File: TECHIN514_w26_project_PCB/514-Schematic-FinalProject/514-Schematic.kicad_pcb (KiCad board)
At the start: 2 copper layers, 138 x 62 mm, 15 parts, among them J1 Conn_01x02, U1 28BYJ-48, U2 MPU-6050, U3 ULN2003, U4 ESP32C3, U5 ESP32C3, U6 SSD1306

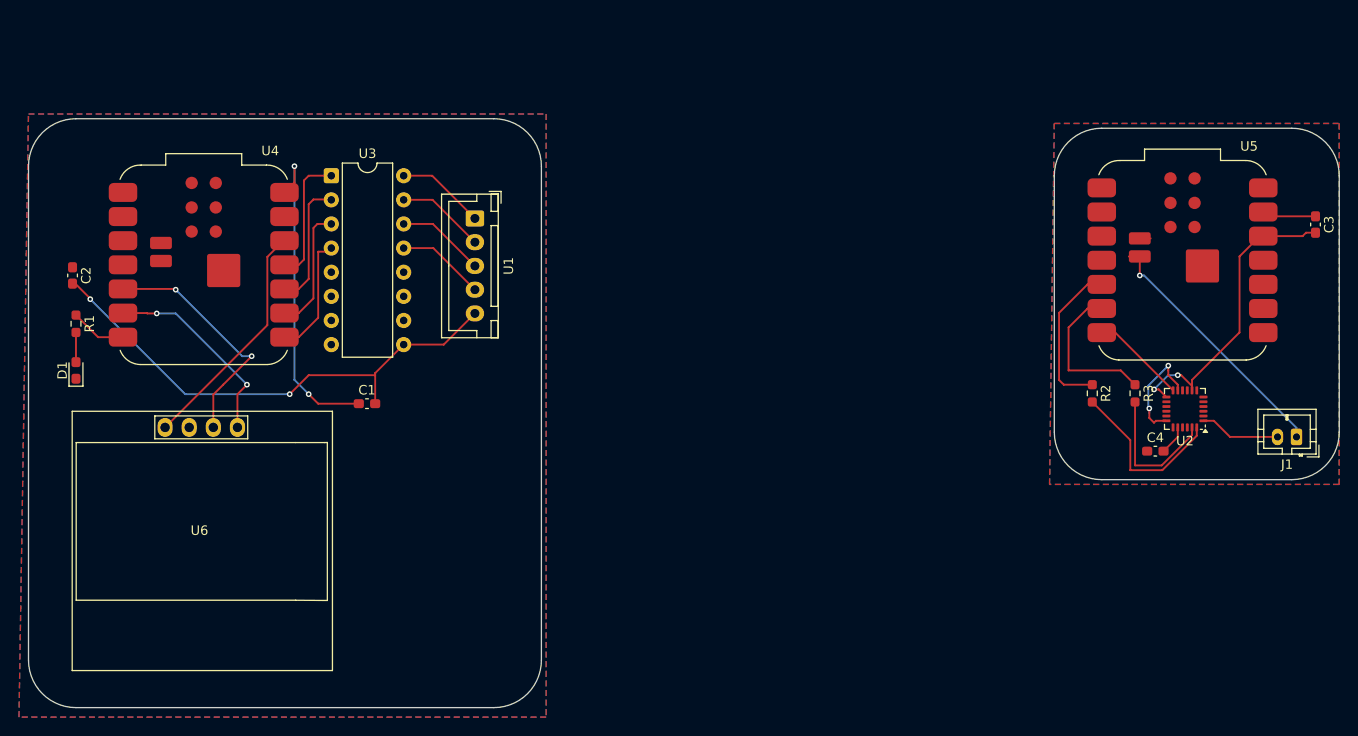
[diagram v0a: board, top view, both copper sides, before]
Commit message: Add PCB and Code for Devices
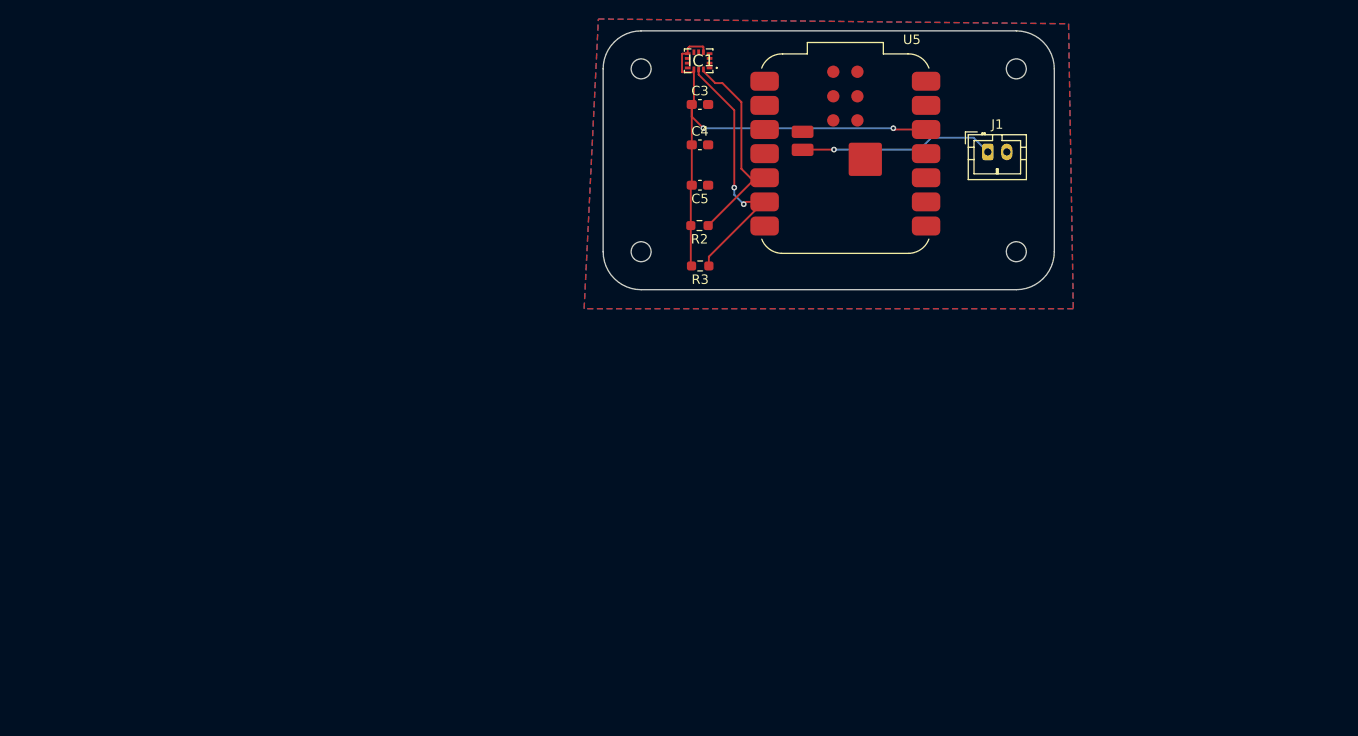
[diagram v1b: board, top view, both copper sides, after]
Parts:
- removed C1: 470uF, Capacitor_SMD:C_0603_1608Metric_Pad1.08x0.95mm_HandSolder
- removed C2: 0.1 uF, Capacitor_SMD:C_0603_1608Metric_Pad1.08x0.95mm_HandSolder
- removed D1: LED, LED_SMD:LED_0603_1608Metric_Pad1.05x0.95mm_HandSolder
- removed R1: 330V, Resistor_SMD:R_0603_1608Metric_Pad0.98x0.95mm_HandSolder
- removed U1: 28BYJ-48, Connector_JST:JST_XH_B5B-XH-A_1x05_P2.50mm_Vertical
- removed U2: MPU-6050, Sensor_Motion:InvenSense_QFN-24_4x4mm_P0.5mm
- removed U3: ULN2003, Package_DIP:DIP-16_W7.62mm
- removed U4: ESP32C3, RF_Module:MCU_Seeed_ESP32C3
- removed U6: SSD1306, Footprints:128x64OLED
- added C5: 10 nF, Capacitor_SMD:C_0603_1608Metric_Pad1.08x0.95mm_HandSolder, F.Cu at (177.7, 66.0)
- added IC1: ICM-42670-P, IMU:ICM42670P, F.Cu at (177.6, 52.9)
- added REF**: MountingHole_2.1mm, MountingHole:MountingHole_2.1mm, F.Cu at (171.5, 53.8)
- added REF**: MountingHole_2.1mm, MountingHole:MountingHole_2.1mm, F.Cu at (211.0, 73.0)
- added REF**: MountingHole_2.1mm, MountingHole:MountingHole_2.1mm, F.Cu at (171.5, 73.0)
- added REF**: MountingHole_2.1mm, MountingHole:MountingHole_2.1mm, F.Cu at (211.0, 53.8)
- C4: value 2.2 nF -> 2.2 uF
- R2, R3: value 4.7k -> 10 kΩ
- moved C3 66.0 mm to (177.7, 57.5), turned to 0 degrees
- moved C4 57.8 mm to (177.7, 61.8)
- moved R3 47.7 mm to (177.7, 74.5), turned to 180 degrees
- moved R2 45.0 mm to (177.6, 70.2), turned to 180 degrees
- moved J1 44.2 mm to (208.0, 62.5), turned to 0 degrees
- moved U5 37.2 mm to (193.0, 62.7)
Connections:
- C3 pad 1: Net-(U5-GND) -> Net-(IC1-AP_CS)
- C3 pad 2: Net-(U2-VDD) -> GND
- C4 pad 1: GND -> Net-(IC1-AP_CS)
- C4 pad 2: Net-(U2-CPOUT) -> GND
- R2 pad 2: Net-(U2-SDA) -> Net-(IC1-AP_CS)
- R3 pad 2: Net-(U2-SCL) -> Net-(IC1-AP_CS)
- U5 pad 12: Net-(U2-VDD) -> Net-(IC1-AP_CS)
- U5 pad 13: Net-(U5-GND) -> unconnected-(U5-GND-Pad13)
- U5 pad 7: Net-(U2-INT) -> unconnected-(U5-D6-Pad7)
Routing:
- net Net-(IC1-AP_CS): track 0.00 -> 54.3 mm, vias 0 -> 2
- net Net-(U1-VCC): track 53.9 -> 0.00 mm, vias 2 -> 0
- net Net-(U4-5V): track 33.5 -> 0.00 mm, vias 2 -> 0
- net Net-(U2-VDD): track 32.4 -> 0.00 mm, vias 2 -> 0
- net Net-(U4-D4): track 25.7 -> 0.00 mm, vias 2 -> 0
- net +3V3: track 24.9 -> 0.00 mm
- net GND: track 21.7 -> 0.00 mm, vias 2 -> 0
- net Net-(U4-D5): track 21.1 -> 0.00 mm, vias 2 -> 0
- net Net-(U2-SDA): track 18.2 -> 0.00 mm
- net Net-(U2-SCL): track 14.8 -> 0.00 mm
- net Net-(U3-I1): track 13.7 -> 0.00 mm
- net Net-(U3-I2): track 13.5 -> 0.00 mm
- net Net-(U3-I3): track 13.2 -> 0.00 mm
- net Net-(U3-I4): track 12.9 -> 0.00 mm
- net Net-(IC1-AP_SCL_/_AP_SCLK): track 16.5 -> 27.7 mm, vias 0 -> 2
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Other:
- board size 138 x 62 mm -> 47.5 x 27.2 mm
